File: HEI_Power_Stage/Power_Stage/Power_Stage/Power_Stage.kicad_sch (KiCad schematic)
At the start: 1 part, among them Q1 EPC2304ENGRT

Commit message: second try for kicad libs
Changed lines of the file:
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@@
 (kicad_sch (version 20230121) (generator eeschema)
   (paper "A4")
-  (symbol (lib_id "GTSR_symbol_lib_SD:EPC2304ENGRT") (at 150.495 96.52 0) (unit 1)
+  (symbol (lib_id "GTSR_symbol_lib_SD:EPC2304ENGRT") (at 153.67 92.71 0) (unit 1)
     (in_bom yes) (on_board yes) (dnp no) (fields_autoplaced)
-    (property "Reference" "Q1" (at 150.495 95.25 0)
+    (property "Reference" "Q1" (at 153.67 91.44 0)
       (effects (font (size 1.27 1.27)))
     )
-    (property "Value" "EPC2304ENGRT" (at 150.495 97.79 0)
+    (property "Value" "EPC2304ENGRT" (at 153.67 93.98 0)
       (effects (font (size 1.27 1.27)))
     )
-    (property "Footprint" "GTSR_KiCAD_Footprints_SD:EPC2304_ECC" (at 150.495 96.52 0)
+    (property "Footprint" "GTSR_KiCAD_Footprints_SD:EPC2304_ECC" (at 153.67 92.71 0)
       (effects (font (size 1.27 1.27)) hide)
     )
-    (property "Datasheet" "https://www.digikey.com/en/products/detail/epc/EPC2304ENGRT/16785484" (at 150.495 96.52 0)
+    (property "Datasheet" "https://www.digikey.com/en/products/detail/epc/EPC2304ENGRT/16785484" (at 153.67 92.71 0)
       (effects (font (size 1.27 1.27)) hide)
     )

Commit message: preliminary schematic and layout for POC
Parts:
- removed Q1: EPC2304ENGRT, GTSR_KiCAD_Footprints_SD:EPC2304_ECC, symbol GTSR_symbol_lib_SD:EPC2304ENGRT
- added C1 (x3): 3.3uF, GTSR_KiCAD_Footprints:CAP_6050_TDK, symbol Device:C
- added C44, C46, C6, C7, C8: 10uF, Capacitor_SMD:C_0603_1608Metric_Pad1.08x0.95mm_HandSolder, symbol Device:C
- added D14 (x2): G, LED_SMD:LED_0603_1608Metric_Pad1.05x0.95mm_HandSolder, symbol Device:LED
- added H2 (x4): No. 8, MountingHole:MountingHole_2.1mm, symbol Mechanical:MountingHole
- added J2: Conn_02x10_Odd_Even, Connector_PinSocket_2.54mm:PinSocket_2x10_P2.54mm_Horizontal, symbol Connector_Generic:Conn_02x10_Odd_Even
- added J3, J4, J5: Screw_Terminal_01x01, GTSR_KiCAD_Footprints_SD:CONN6_1057_WRE, symbol Connector:Screw_Terminal_01x01
- added J5: OSTTA020161, GTSR_KiCAD_Footprints:CONN_OSTTA020161_OST, symbol GTSR_symbol_lib:OSTTA020161
- added R69: 440, Resistor_SMD:R_0603_1608Metric_Pad0.98x0.95mm_HandSolder, symbol Device:R_US
- added R69: 1.8k, Resistor_SMD:R_0603_1608Metric_Pad0.98x0.95mm_HandSolder, symbol Device:R_US
- added TP1, TP2, TP3, TP4: Test_Point, TestPoint:TestPoint_Pad_D1.0mm, symbol GTSR_symbol_lib:Test_Point
- added U1: TBA 2-1212, GTSR_KiCAD_Footprints_SD:TBA 2_SINGLE_TRP, symbol GTSR_symbol_lib_SD:TBA_2-1212
- added U2: 1769205241, GTSR_KiCAD_Footprints_SD:176920512, symbol TRV 2:TRV_2
- added U3: TPS73250DBVR, Package_TO_SOT_SMD:TSOT-23-5, symbol Regulator_Linear:AMS1117-1.8
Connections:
- new net: D14.1 (K), R69.2
- new net: D14.2 (A), R69.1
- new net +12V: C44.1, C46.1, C6.1, D14.2 (A), J2.19 (Pin_19), TP1.1, TP3.1, U1.1 (+VIN(VCC)), U1.6 (+VOUT), U2.2 (Vin+)
- new net +5V: C7.1, C8.1, J2.16 (Pin_16), R69.2, U2.5 (Vout+), U3.1 (VI), U3.3 (EN)
- new net 5Vref: U3.5 (VO)
- new net AHS_{PWM}: J2.9 (Pin_9)
- new net ALS_{PWM}: J2.11 (Pin_11)
- new net A~{CS}: J2.8 (Pin_8)
- new net BHS_{PWM}: J2.5 (Pin_5)
- new net BLS_{PWM}: J2.7 (Pin_7)
- new net B~{CS}: J2.6 (Pin_6)
- new net CHS_{PWM}: J2.1 (Pin_1)
- new net CLK: J2.14 (Pin_14)
- new net CLS_{PWM}: J2.3 (Pin_3)
- new net C~{CS}: J2.4 (Pin_4)
- new net GND: C46.2, J2.17 (Pin_17), R69.1, TP4.1, U1.4 (-VOUT)
- new net GNDPWR: C1.2, C1.2, C1.2, C7.2, C8.2, D14.1 (K), J2.18 (Pin_18), J5.2, U2.4 (Vout-), U3.2 (GND)
- new net GND_LV: C44.2, C6.2, J2.20 (Pin_20), TP2.1, U1.2 (-VIN(GND)), U2.1 (Vin-)
- new net MISO: J2.12 (Pin_12)
- new net MOSI: J2.10 (Pin_10)
- new net PHA: J3.1 (Pin_1), J3.2 (Pin_1), J3.3 (Pin_1), J3.4 (Pin_1), J3.5 (Pin_1), J3.6 (Pin_1)
- new net PHB: J4.1 (Pin_1), J4.2 (Pin_1), J4.3 (Pin_1), J4.4 (Pin_1), J4.5 (Pin_1), J4.6 (Pin_1)
- new net PHC: J5.1 (Pin_1), J5.2 (Pin_1), J5.3 (Pin_1), J5.4 (Pin_1), J5.5 (Pin_1), J5.6 (Pin_1)
- new net VDC: C1.1, C1.1, C1.1, J5.1
- no-connect marks 0 -> 3
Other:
- added sheet Phase1 (Phase.kicad_sch)
- added sheet Phase2 (Phase.kicad_sch)
- added sheet Phase3 (Phase.kicad_sch)
- note added: "12 -ISO-> 12"
- note added: "12 -ISO-> 5"
- note added: "5 -> 5Vref"
- note added: "Add more capacitance"
- note added: "Add more testpoints"
- note added: "CLCB Connector"
- note added: "Connectors + Bulk Capacitance"
- note added: "Gate Driver Supply (Isolated)"
- note added: "Half Bridges + Gate Drivers"
- note added: "No iso 12V for now"
- note added: "Probably makes sense to leave gate drivers always enabled"
- note added: "Sensing Supply + Ref (GNDPWR)"
- title: (none) -> High Efficiency Inverter

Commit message: changes in meeting
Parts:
- C44, C46, D14, R69, TP3, TP4, U1: now fitted; now in the parts list
- J2: footprint Connector_PinSocket_2.54mm:PinSocket_2x10_P2.54mm_Horizontal -> Connector_PinHeader_2.54mm:PinHeader_2x10_P2.54mm_Horizontal
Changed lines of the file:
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@@
 		(unit 1)
 		(exclude_from_sim no)
-		(in_bom no)
-		(on_board no)
-		(dnp yes)
+		(in_bom yes)
+		(on_board yes)
+		(dnp no)
 		(property "Reference" "C44"
 			(at 79.375 60.96 0)
@@
 		(unit 1)
 		(exclude_from_sim no)
-		(in_bom no)
-		(on_board no)
-		(dnp yes)
+		(in_bom yes)
+		(on_board yes)
+		(dnp no)
 		(property "Reference" "D14"
 			(at 163.195 57.4674 90)
@@
 		(unit 1)
 		(exclude_from_sim no)
-		(in_bom no)
-		(on_board no)
-		(dnp yes)
+		(in_bom yes)
+		(on_board yes)
+		(dnp no)
 		(property "Reference" "TP4"
 			(at 135.89 71.12 0)
@@
 		(unit 1)
 		(exclude_from_sim no)
-		(in_bom no)
-		(on_board no)
-		(dnp yes)
+		(in_bom yes)
+		(on_board yes)
+		(dnp no)
 		(property "Reference" "R69"
 			(at 162.56 65.405 90)
@@
 		(unit 1)
 		(exclude_from_sim no)
-		(in_bom no)
-		(on_board no)
-		(dnp yes)
+		(in_bom yes)
+		(on_board yes)
+		(dnp no)
 		(property "Reference" "TP3"
 			(at 135.89 53.34 0)
@@
 		(unit 1)
 		(exclude_from_sim no)
-		(in_bom no)
-		(on_board no)
-		(dnp yes)
+		(in_bom yes)
+		(on_board yes)
+		(dnp no)
 		(property "Reference" "U1"
 			(at 113.03 55.88 0)
@@
 			)
 		)
-		(property "Footprint" "Connector_PinSocket_2.54mm:PinSocket_2x10_P2.54mm_Horizontal"
+		(property "Footprint" "Connector_PinHeader_2.54mm:PinHeader_2x10_P2.54mm_Horizontal"
 			(at 40.005 60.325 0)
 			(effects
@@
 		(unit 1)
 		(exclude_from_sim no)
-		(in_bom no)
-		(on_board no)
-		(dnp yes)
+		(in_bom yes)
+		(on_board yes)
+		(dnp no)
 		(property "Reference" "C46"
 			(at 140.97 60.96 0)

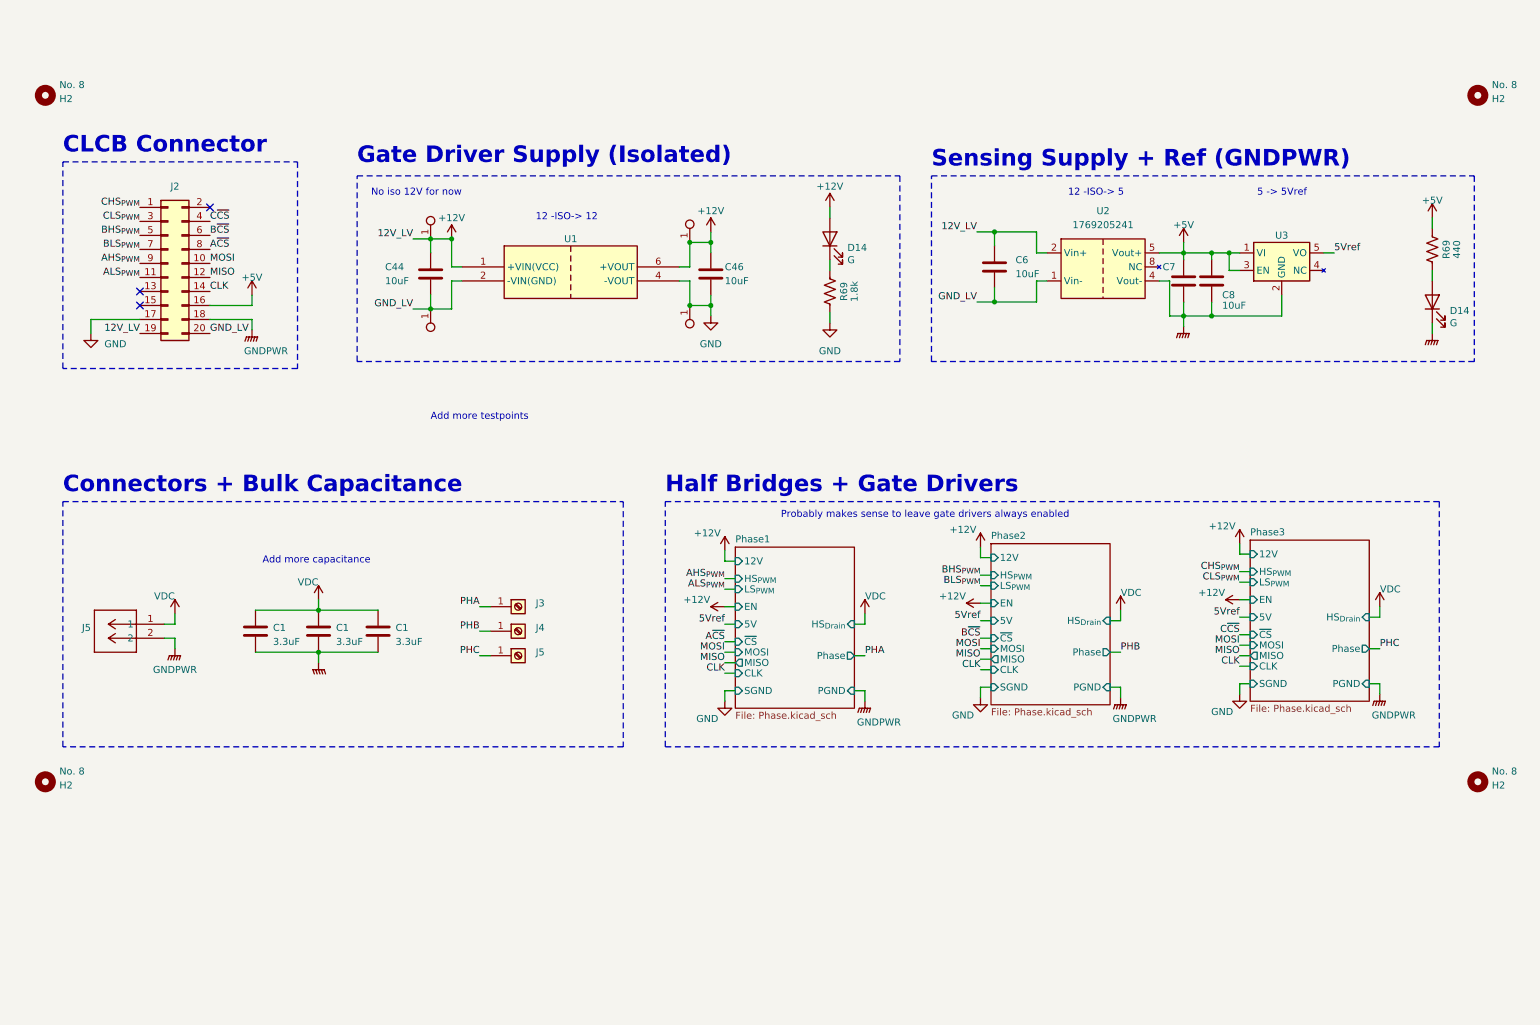
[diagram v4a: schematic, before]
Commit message: layout
5v regulators for each phase daq
12v iso
top half and bottom half planes
SPi goes from bottom to top layer at plane split
power routed on bottom two layers with solid planes
switch nodes on top two layers
4 adcs now
daq for dc input
current sensors now references to gndpwr
Still need to figure out how to connect gndpwr pours with isolation
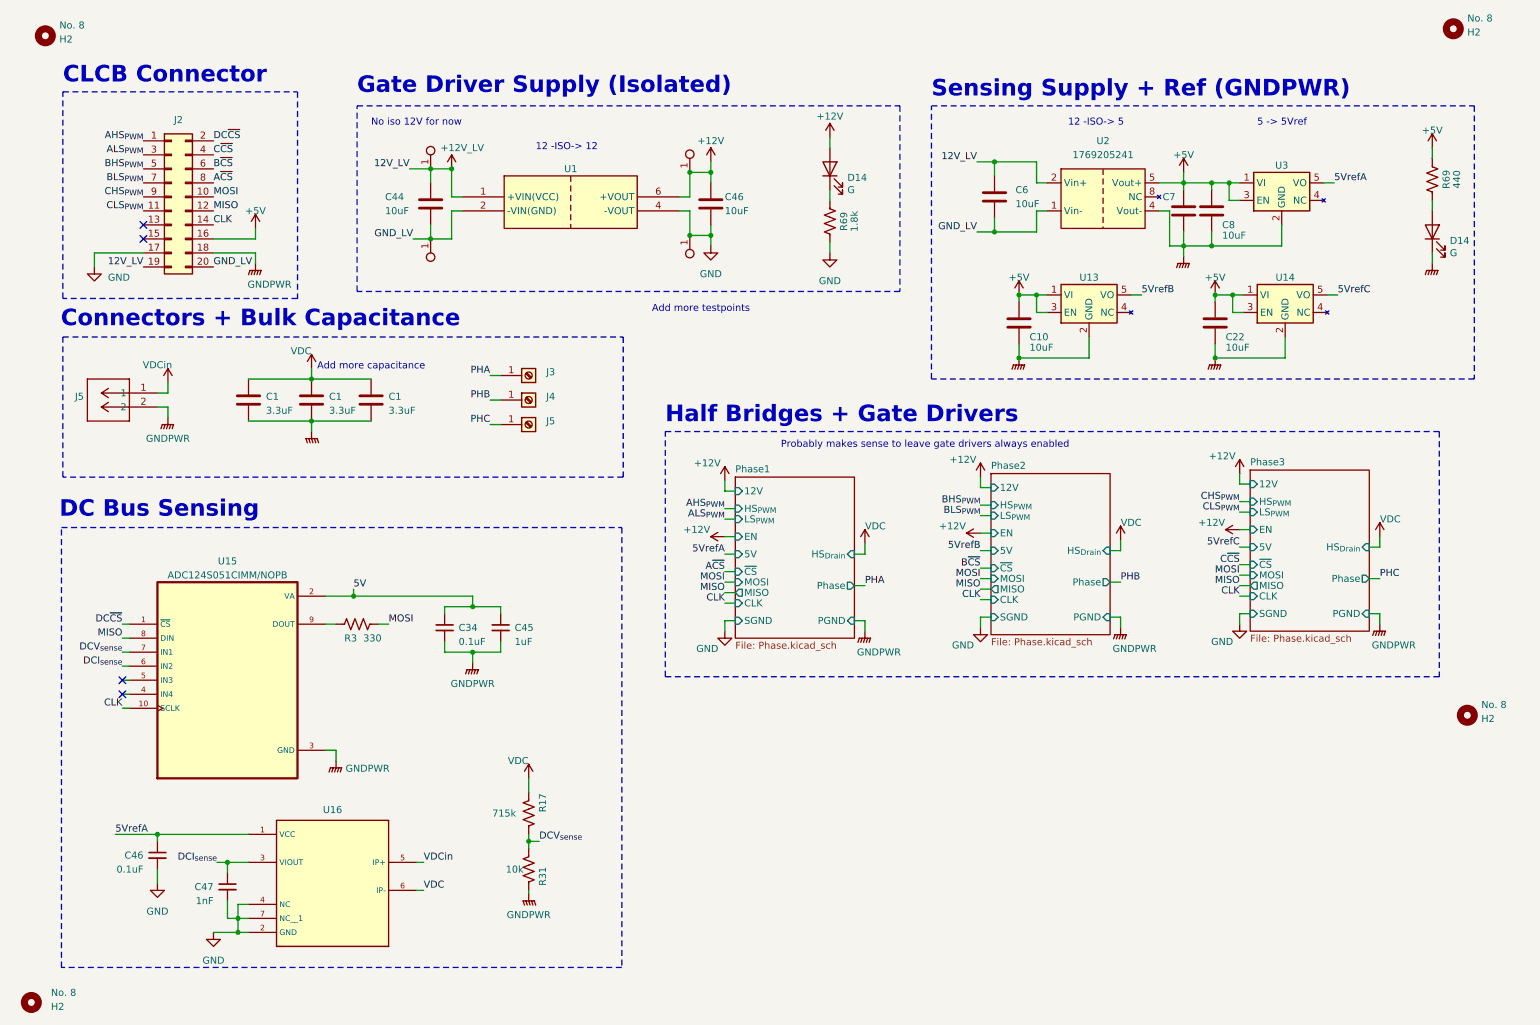
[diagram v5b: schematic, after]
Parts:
- added C10, C22: 10uF, Capacitor_SMD:C_0603_1608Metric_Pad1.08x0.95mm_HandSolder, symbol Device:C
- added C34, C46: 0.1uF, Capacitor_SMD:C_0603_1608Metric_Pad1.08x0.95mm_HandSolder, symbol Device:C_Small
- added C45: 1uF, Capacitor_SMD:C_0603_1608Metric_Pad1.08x0.95mm_HandSolder, symbol Device:C_Small
- added C47: 1nF, Capacitor_SMD:C_0603_1608Metric_Pad1.08x0.95mm_HandSolder, symbol Device:C_Small
- added R17: 715k, Resistor_SMD:R_1206_3216Metric, symbol Device:R_US
- added R3: 330, Resistor_SMD:R_0603_1608Metric_Pad0.98x0.95mm_HandSolder, symbol Device:R_US
- added R31: 10k, Resistor_SMD:R_1206_3216Metric, symbol Device:R_US
- added U13, U14: TPS73250DBVR, Package_TO_SOT_SMD:TSOT-23-5, symbol Regulator_Linear:AMS1117-1.8
- added U15: ADC124S051CIMM/NOPB, GTSR:SOP50P490X110-10N, symbol GTSR_symbol_lib_SD:ADC124S021CIMMX/NOPB
- added U16: ~, GTSR:XDCR_ACS72981LLRATR-100B5, symbol GTSR_symbol_lib_SD:ACS72981LLRATR-100B5
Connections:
- net +12V: no longer C44.1, C6.1, J2.19 (Pin_19), TP1.1, U1.1 (+VIN(VCC)), U2.2 (Vin+)
- net +5V: now also C10.1, C22.1, U13.1 (VI), U13.3 (EN), U14.1 (VI), U14.3 (EN)
- net AHS_{PWM}: now also J2.1 (Pin_1); no longer J2.9 (Pin_9)
- net ALS_{PWM}: now also J2.3 (Pin_3); no longer J2.11 (Pin_11)
- net CHS_{PWM}: now also J2.9 (Pin_9); no longer J2.1 (Pin_1)
- net CLK: now also U15.10 (SCLK)
- net CLS_{PWM}: now also J2.11 (Pin_11); no longer J2.3 (Pin_3)
- net GND: now also C46.2, C47.2, U16.2 (GND), U16.4 (NC), U16.7 (NC__1)
- net GNDPWR: now also C10.2, C22.2, C34.2, C45.2, R31.1, U13.2 (GND), U14.2 (GND), U15.3 (GND)
- net MISO: now also U15.8 (DIN)
- net MOSI: now also R3.2
- net VDC: now also R17.2, U16.6 (IP-); no longer J5.1
- net DC~{CS}: now reaches J2.2 (Pin_2)
- net DC~{CS}: now also U15.1 (~{CS})
- net 5Vref renamed 5VrefA
- net 5VrefA: now also C46.1, U16.1 (VCC)
- new net: R3.1, U15.9 (DOUT)
- new net +12V_LV: C44.1, C6.1, J2.19 (Pin_19), TP1.1, U1.1 (+VIN(VCC)), U2.2 (Vin+)
- new net 5V: C34.1, C45.1, U15.2 (VA)
- new net 5VrefB: U13.5 (VO)
- new net 5VrefC: U14.5 (VO)
- new net DCI_{sense}: C47.1, U15.6 (IN2), U16.3 (VIOUT)
- new net DCV_{sense}: R17.1, R31.2, U15.7 (IN1)
- new net VDCin: J5.1, U16.5 (IP+)
- no-connect marks 3 -> 4
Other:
- note added: "DC Bus Sensing"
- moved on the sheet: C1, C44, C46, C6, C7, C8, D14, H2, J2, J3, J4, J5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

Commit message: changes since class on friday
solid gndpwr plane on layer 3
new cap... its large
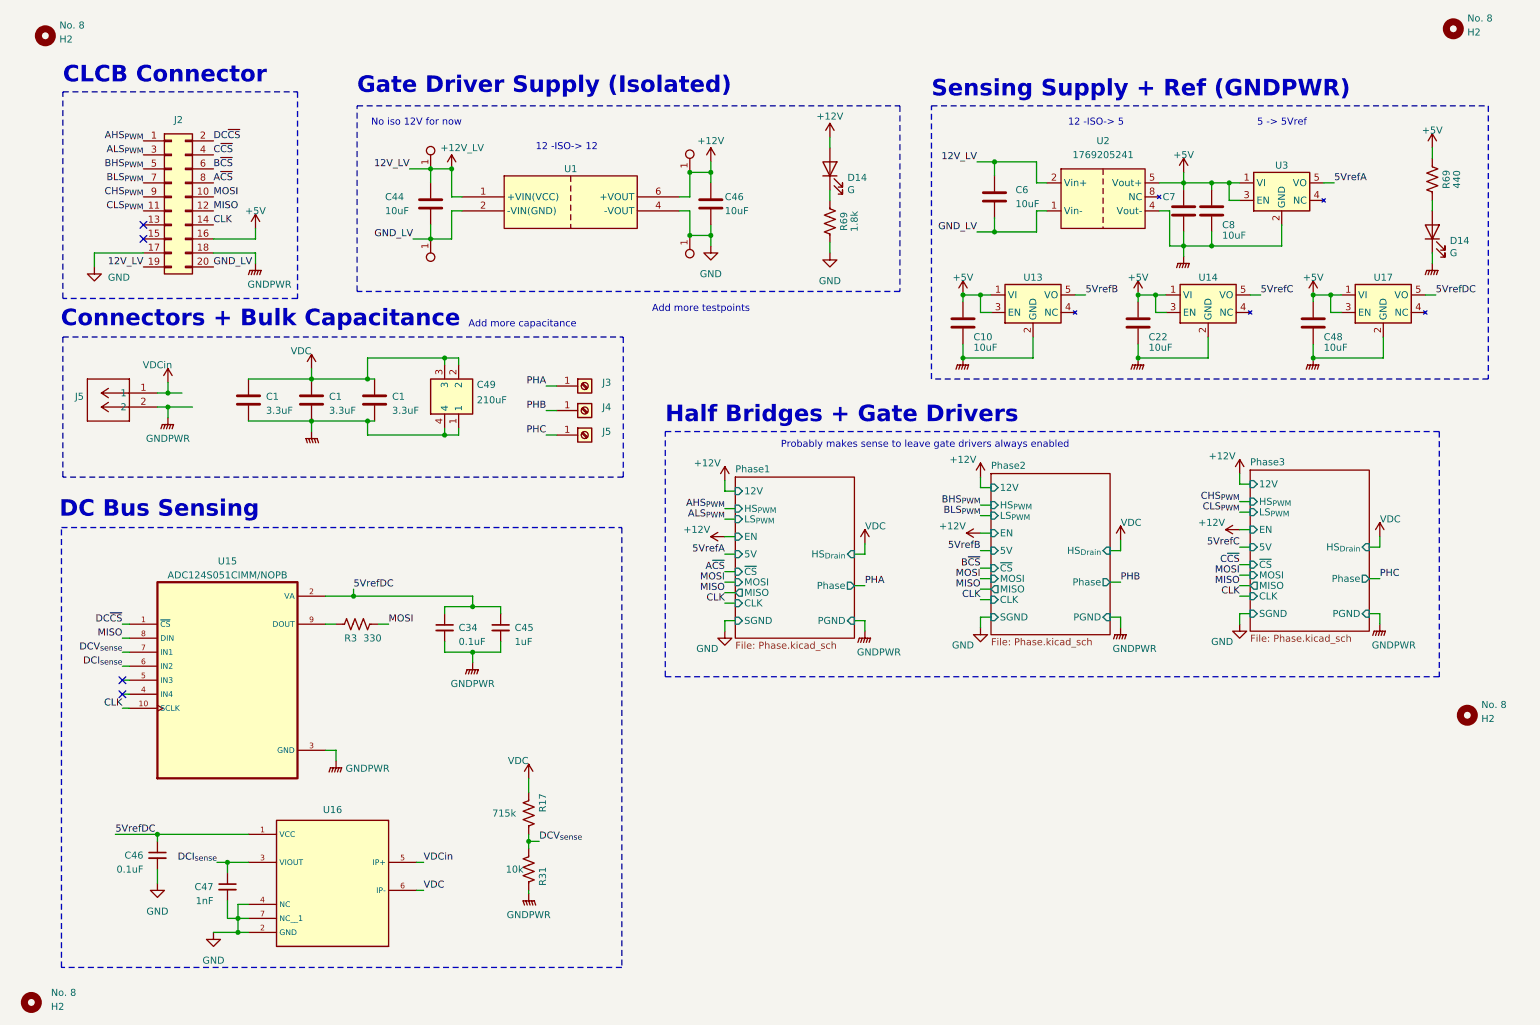
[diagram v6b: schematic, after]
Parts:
- added C48: 10uF, Capacitor_SMD:C_0603_1608Metric_Pad1.08x0.95mm_HandSolder, symbol Device:C
- added C49: 210uF, C4AQLEW6210A3BK, symbol kemet_cap:C4AQLEW6210A3BK
- added U17: TPS73250DBVR, Package_TO_SOT_SMD:TSOT-23-5, symbol Regulator_Linear:AMS1117-1.8
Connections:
- net +5V: now also C48.1, U17.1 (VI), U17.3 (EN)
- net 5VrefA: no longer C46.1, U16.1 (VCC)
- net GNDPWR: now also C48.2, C49.1, C49.4, U17.2 (GND)
- net VDC: now also C49.2, C49.3
- net 5V renamed 5VrefDC
- net 5VrefDC: now also C46.1, U16.1 (VCC), U17.5 (VO)
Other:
- moved on the sheet: C1, C10, C22, J3, J4, J5, U13, U14
